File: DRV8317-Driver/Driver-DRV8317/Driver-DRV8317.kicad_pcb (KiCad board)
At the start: 4 copper layers, 55 x 81 mm, 50 parts, among them IC3 DRV8317HREER, J1 Conn_02x13_Odd_Even, J5 Jack-DC, J6 Screw_Terminal_01x03, U1 LM2596S-ADJ, U2 LM2674M-5.0, U3 LD1117S33TR

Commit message: kncoadsnofijasndvoi
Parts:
- added D5: Red LED, LED_SMD:LED_0805_2012Metric, F.Cu at (120.3, 81.0)
- added R34: 3.6, Resistor_SMD:R_0805_2012Metric, F.Cu at (117.2, 82.2)
- added R35: 3.6, Resistor_SMD:R_0805_2012Metric, F.Cu at (117.2, 80.0)
- R42: footprint Resistor_SMD:R_0603_1608Metric -> Resistor_SMD:R_0805_2012Metric
- moved R42 3.49 mm to (96.1, 99.8), turned to 180 degrees
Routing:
- net AVDD: track 47.3 -> 51.1 mm, vias 24 -> 25
- net Net-(D5-A): track 0.00 -> 2.25 mm
- net Net-(R34-Pad2): track 0.00 -> 2.11 mm
- net GND: track 83.1 -> 85.0 mm, vias 137 -> 138

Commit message: Up
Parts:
- added C33: 22pF, Capacitor_SMD:C_0603_1608Metric, F.Cu at (107.0, 101.0)
- added C34: 22pF, Capacitor_SMD:C_0603_1608Metric, F.Cu at (103.7, 101.0)
- added C35: 22pF, Capacitor_SMD:C_0603_1608Metric, F.Cu at (100.5, 101.0)
- added D6: Red LED, LED_SMD:LED_0805_2012Metric, F.Cu at (120.3, 86.3)
- added R36: 3.6, Resistor_SMD:R_0805_2012Metric, F.Cu at (120.3, 90.1)
- added R37: 3.6, Resistor_SMD:R_0805_2012Metric, F.Cu at (118.2, 88.2)
- added R4: 330, Resistor_SMD:R_0603_1608Metric, F.Cu at (107.0, 99.5)
- added R5: 330, Resistor_SMD:R_0603_1608Metric, F.Cu at (103.8, 99.5)
- added R6: 330, Resistor_SMD:R_0603_1608Metric, F.Cu at (100.5, 99.4)
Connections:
- J1 pad 5: /DRV8317/Vcurrfdbk_A -> Net-(J1-Pin_5)
- J1 pad 7: /DRV8317/Vcurrfdbk_B -> Net-(J1-Pin_7)
- J1 pad 9: /DRV8317/Vcurrfdbk_C -> Net-(J1-Pin_9)
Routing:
- net /DRV8317/NFAULT: track 23.7 -> 70.0 mm
- net GND: track 85.0 -> 92.8 mm, vias 138 -> 139
- net /DRV8317/Vcurrfdbk_B: track 22.3 -> 14.7 mm
- net /DRV8317/Vcurrfdbk_C: track 19.0 -> 11.7 mm
- net Net-(J1-Pin_5): track 0.00 -> 6.92 mm
- net Net-(J1-Pin_7): track 0.00 -> 6.78 mm
- net Net-(J1-Pin_9): track 0.00 -> 6.36 mm
- net /DRV8317/Vcurrfdbk_A: track 23.9 -> 18.1 mm
- net Net-(D6-A): track 0.00 -> 2.12 mm
- net Net-(R36-Pad2): track 0.00 -> 2.08 mm
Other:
- board text added: "NFAULT"
- board text added: "PWR"

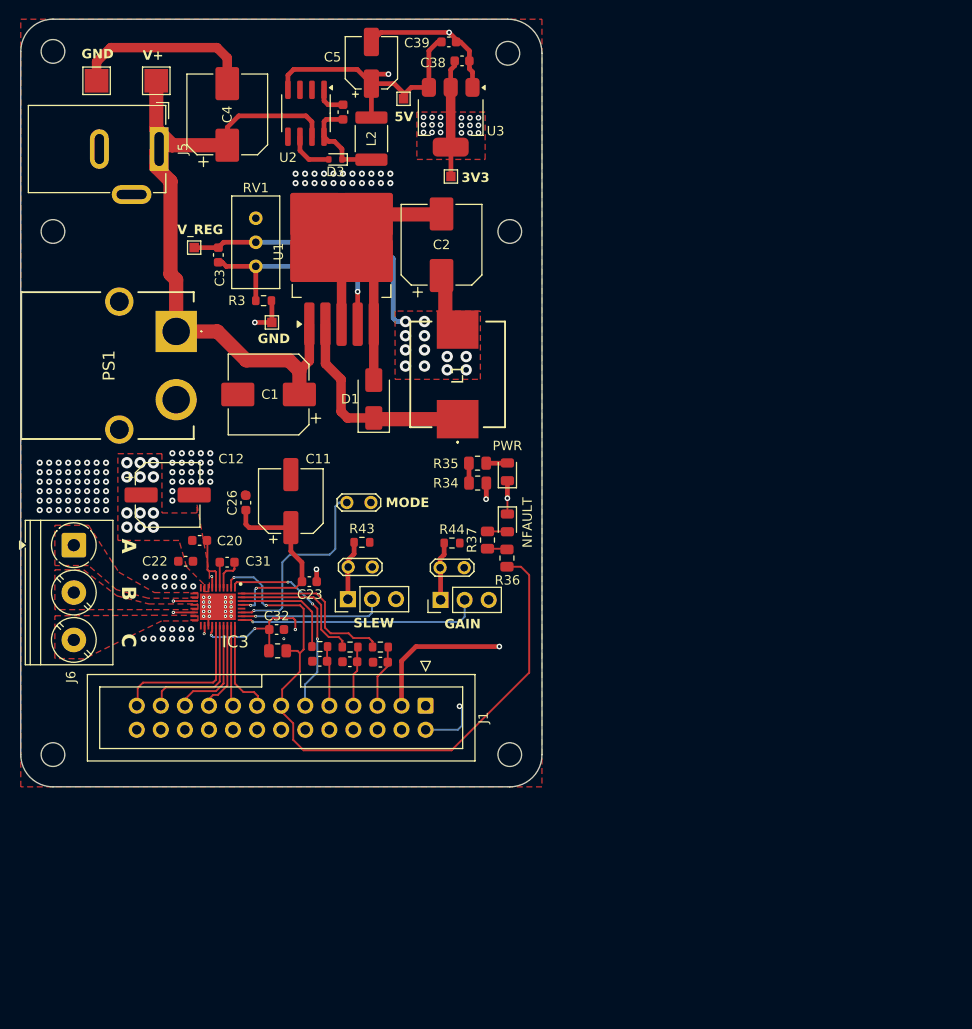
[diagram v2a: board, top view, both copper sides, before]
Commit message: fix all via to 0.45/0.3 mm
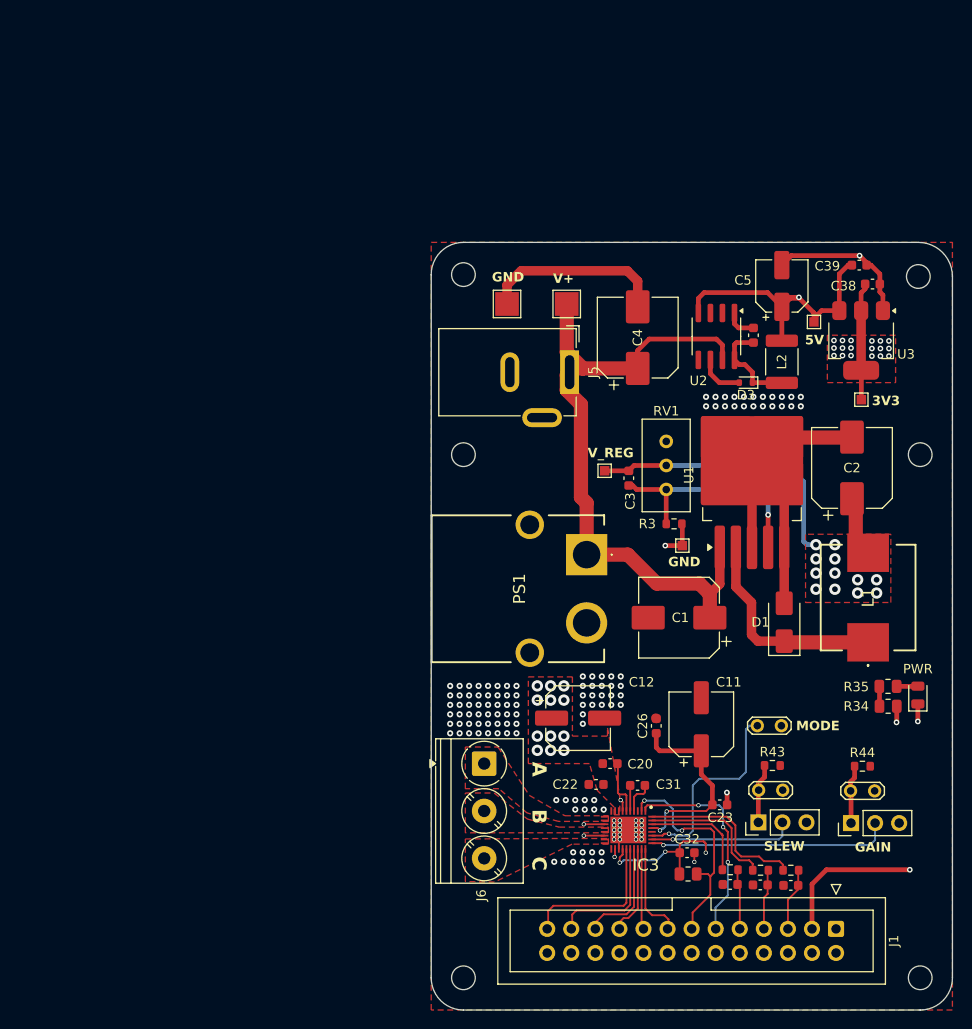
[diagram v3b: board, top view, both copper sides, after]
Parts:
- removed D6: Red LED, LED_SMD:LED_0805_2012Metric
- removed R36, R37: 3.6, Resistor_SMD:R_0805_2012Metric
- moved C35 49.3 mm to (143.9, 124.5)
- moved IC3 49.3 mm to (133.1, 118.8)
- moved JP2 49.3 mm to (156.6, 118.0)
- moved JP4 49.3 mm to (146.8, 118.0)
- moved JP5 49.3 mm to (146.9, 114.5)
- moved R6 49.3 mm to (143.9, 123.0)
- moved RV1 49.3 mm to (137.1, 82.8)
- moved TP1 49.3 mm to (130.6, 80.8)
- moved U3 49.3 mm to (157.7, 67.1)
- moved C26 49.3 mm to (136.1, 107.8)
- moved C32 49.3 mm to (139.3, 121.2)
- moved R42 49.3 mm to (139.4, 123.4)
- moved R44 49.3 mm to (157.8, 112.0)
- moved C1 49.3 mm to (138.5, 96.3)
- moved C11 49.3 mm to (140.8, 107.6)
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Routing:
- net /DRV8317/NFAULT: track 70.0 -> 24.2 mm
- net GND: track 92.8 -> 85.9 mm, vias 139 -> 138
- net Net-(D6-A): track 2.12 -> 0.00 mm
- net Net-(R36-Pad2): track 2.08 -> 0.00 mm
- net /DRV8317/NSLEEP: track 21.4 -> 22.5 mm
- net +5V: track 119.8 -> 120.8 mm
- net AVDD: track 51.1 -> 52.0 mm
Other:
- board text removed: "NFAULT"
